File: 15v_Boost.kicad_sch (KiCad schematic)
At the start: 6 parts, among them U6 LMR62421XMF

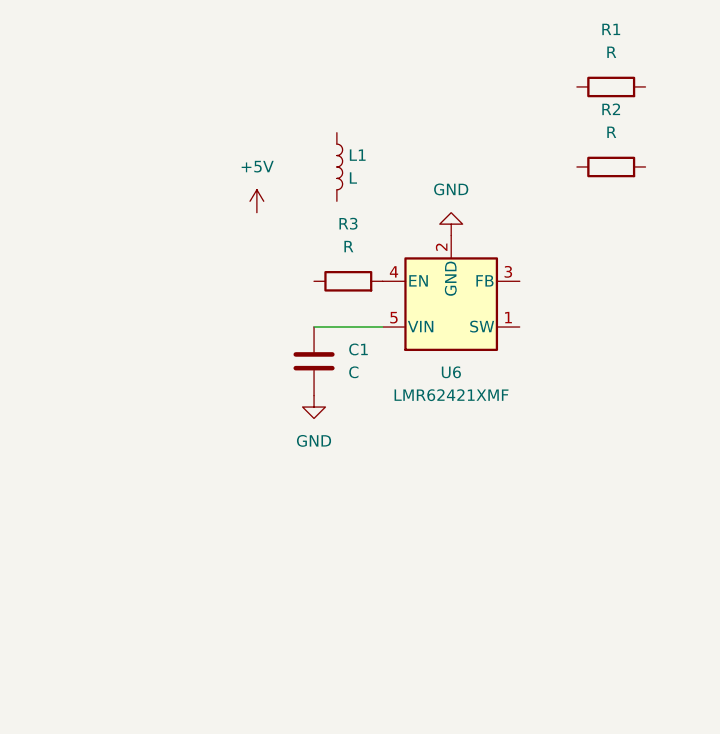
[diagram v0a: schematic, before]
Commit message: finalized schematic ready for layout
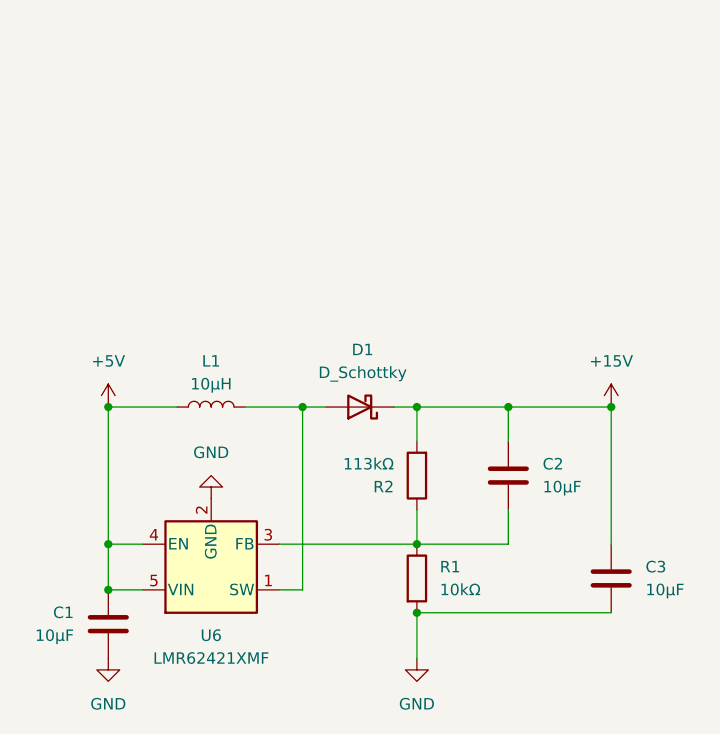
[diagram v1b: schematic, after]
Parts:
- removed R3: R, symbol Device:R
- added C2, C3: 10µF, Capacitor_THT:CP_Radial_D10.0mm_P5.00mm, symbol Device:C
- added D1: D_Schottky, Diode_SMD:D_SMA_Handsoldering, symbol Device:D_Schottky
- C1: value C -> 10µF; footprint (none) -> Capacitor_THT:CP_Radial_D10.0mm_P5.00mm; URL (none) -> https://www.digikey.com/en/products/detail/chemi-con/KTD500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
- L1: value L -> 10µH; footprint (none) -> Inductor_THT:L_Radial_D7.5mm_P5.00mm_Fastron_07P; URL (none) -> https://www.digikey.com/en/products/detail/kemet/SBC1-100-1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
- R1: value R -> 10kΩ; footprint (none) -> Resistor_THT:R_Axial_DIN0207_L6.3mm_D2.5mm_P7.62mm_Horizontal; URL (none) -> https://www.digikey.com/en/products/detail/stackpole-electr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
- R2: value R -> 113kΩ; footprint (none) -> Resistor_THT:R_Axial_DIN0207_L6.3mm_D2.5mm_P7.62mm_Horizontal; URL (none) -> https://www.digikey.com/en/products/detail/stackpole-electr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
- U6: URL (none) -> https://www.digikey.com/en/products/detail/texas-instrument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
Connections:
- net +5V: now also C1.1, L1.1, U6.4 (EN), U6.5 (VIN)
- net GND: now also R1.2, C3.2
- net at R2.1: now also R1.1, U6.3 (FB), C2.2
- net +15V: now reaches R2.2
- net +15V: now also C2.1, C3.1, D1.1 (K)
- net at L1.2: now also U6.1 (SW), D1.2 (A)
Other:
- moved on the sheet: C1, L1, R1, R2, U6
